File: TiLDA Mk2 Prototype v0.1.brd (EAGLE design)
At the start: 68 x 100 mm, 215 parts, among them IC1 ATSAM3X8EA-AU, IC2 MPU-6050, IC3 SRF-V1.2, IC4 LTC4160, IC5 S25FL216K0PMFI011, IC6 AT45DB161E-SSHFHA (NP), IC7 HMC5883LSMD (NP), IC8 MCP1825T-3302E/DC, J1 ZX62-AB-5PA(11), J2 FCI 62684-401100ALF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

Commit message: Prototype: Part Value updates Gerbers: update to latest PDF: update to latest
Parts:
- C1, C10: value 0805/2.2u/10V/Y5V -> 0805/2u2/10V/Y5V
- C11, C12, C14, C17, C18, C19, C20: value 0805/2.2u/16V/Y5V -> 0805/2u2/16V/Y5V
- C13, C15, C16, C22, C23: value 0805/2.2u/25V/Y5V -> 0805/2u2/25V/Y5V
- C28: value 0603/4u7/10V/Y5V -> 0603/4u7/6V3/Y5V
- C30, C35: value 0805/10u/6.3V/X5R -> 0805/10u/6V3/X5R
- C5: value 0402/2.2n/50V/X7R -> 0402/2n2/50V/X7R
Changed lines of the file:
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@@
 <text x="43.1" y="32.5" size="0.8128" layer="22" ratio="15" rot="MR90">IC7</text>
 <text x="14.1" y="38.8" size="0.8128" layer="22" ratio="15" rot="MR0">IC3</text>
-<text x="12.3" y="4.9" size="0.8128" layer="22" ratio="15" rot="MR90">IC4</text>
+<text x="13" y="5.4" size="0.8128" layer="22" ratio="15" rot="MR90">IC4</text>
 <text x="20.2" y="71.8" size="0.8128" layer="22" ratio="15" rot="MR90">IC5</text>
 <text x="20.2" y="78.4" size="0.8128" layer="22" ratio="15" rot="MR90">IC6</text>
@@
 <element name="J2" library="TiLDA Mk2 Parts" package="62684-401100" value="FCI 62684-401100ALF" x="42.3" y="7.9" rot="MR180"/>
 <element name="R3" library="TiLDA Mk2 Parts" package="R0402-ARDUINO-ROUND" value="0402/0R/5%/(NP)" x="34.1" y="14.2" rot="MR270"/>
-<element name="C10" library="TiLDA Mk2 Parts" package="C0805K" value="0805/2.2u/10V/Y5V" x="34.3" y="17" rot="MR90"/>
-<element name="C11" library="TiLDA Mk2 Parts" package="C0805K" value="0805/2.2u/16V/Y5V" x="36.3" y="15" rot="MR90"/>
-<element name="C12" library="TiLDA Mk2 Parts" package="C0805K" value="0805/2.2u/16V/Y5V" x="36.3" y="19" rot="MR90"/>
-<element name="C13" library="TiLDA Mk2 Parts" package="C0805K" value="0805/2.2u/25V/Y5V" x="36.3" y="22.9" rot="MR90"/>
-<element name="C14" library="TiLDA Mk2 Parts" package="C0805K" value="0805/2.2u/16V/Y5V" x="39.3" y="22.9" rot="MR270"/>
-<element name="C15" library="TiLDA Mk2 Parts" package="C0805K" value="0805/2.2u/25V/Y5V" x="40.3" y="15" rot="MR90"/>
-<element name="C16" library="TiLDA Mk2 Parts" package="C0805K" value="0805/2.2u/25V/Y5V" x="40.3" y="19" rot="MR270"/>
-<element name="C17" library="TiLDA Mk2 Parts" package="C0805K" value="0805/2.2u/16V/Y5V" x="41.3" y="22.9" rot="MR270"/>
-<element name="C18" library="TiLDA Mk2 Parts" package="C0805K" value="0805/2.2u/16V/Y5V" x="43.7" y="15" rot="MR270"/>
-<element name="C19" library="TiLDA Mk2 Parts" package="C0805K" value="0805/2.2u/16V/Y5V" x="43.7" y="18.9" rot="MR270"/>
-<element name="C20" library="TiLDA Mk2 Parts" package="C0805K" value="0805/2.2u/16V/Y5V" x="44.6" y="22" rot="MR0"/>
+<element name="C10" library="TiLDA Mk2 Parts" package="C0805K" value="0805/2u2/10V/Y5V" x="34.3" y="17" rot="MR90"/>
+<element name="C11" library="TiLDA Mk2 Parts" package="C0805K" value="0805/2u2/16V/Y5V" x="36.3" y="15" rot="MR90"/>
+<element name="C12" library="TiLDA Mk2 Parts" package="C0805K" value="0805/2u2/16V/Y5V" x="36.3" y="19" rot="MR90"/>
+<element name="C13" library="TiLDA Mk2 Parts" package="C0805K" value="0805/2u2/25V/Y5V" x="36.3" y="22.9" rot="MR90"/>
+<element name="C14" library="TiLDA Mk2 Parts" package="C0805K" value="0805/2u2/16V/Y5V" x="39.3" y="22.9" rot="MR270"/>
+<element name="C15" library="TiLDA Mk2 Parts" package="C0805K" value="0805/2u2/25V/Y5V" x="40.3" y="15" rot="MR90"/>
+<element name="C16" library="TiLDA Mk2 Parts" package="C0805K" value="0805/2u2/25V/Y5V" x="40.3" y="19" rot="MR270"/>
+<element name="C17" library="TiLDA Mk2 Parts" package="C0805K" value="0805/2u2/16V/Y5V" x="41.3" y="22.9" rot="MR270"/>
+<element name="C18" library="TiLDA Mk2 Parts" package="C0805K" value="0805/2u2/16V/Y5V" x="43.7" y="15" rot="MR270"/>
+<element name="C19" library="TiLDA Mk2 Parts" package="C0805K" value="0805/2u2/16V/Y5V" x="43.7" y="18.9" rot="MR270"/>
+<element name="C20" library="TiLDA Mk2 Parts" package="C0805K" value="0805/2u2/16V/Y5V" x="44.6" y="22" rot="MR0"/>
 <element name="R9" library="TiLDA Mk2 Parts" package="R0402-ARDUINO-ROUND" value="0402/2K/5%" x="46.9" y="12.9" rot="MR270"/>
 <element name="C21" library="TiLDA Mk2 Parts" package="C0603-ROUND" value="0603/1u/10V/X5R" x="47.5" y="16.6" rot="MR90"/>
-<element name="C22" library="TiLDA Mk2 Parts" package="C0805K" value="0805/2.2u/25V/Y5V" x="50.6" y="15.8" rot="MR90"/>
-<element name="C23" library="TiLDA Mk2 Parts" package="C0805K" value="0805/2.2u/25V/Y5V" x="52.55" y="15.8" rot="MR90"/>
+<element name="C22" library="TiLDA Mk2 Parts" package="C0805K" value="0805/2u2/25V/Y5V" x="50.6" y="15.8" rot="MR90"/>
+<element name="C23" library="TiLDA Mk2 Parts" package="C0805K" value="0805/2u2/25V/Y5V" x="52.55" y="15.8" rot="MR90"/>
 <element name="C24" library="TiLDA Mk2 Parts" package="C0603-ROUND" value="0603/1u/10V/X5R" x="54.4" y="12.75" rot="MR180"/>
 <element name="C25" library="TiLDA Mk2 Parts" package="C0603-ROUND" value="0603/1u/10V/X5R" x="56.85" y="12.7" rot="MR90"/>
@@
 <element name="JP6" library="TiLDA Mk2 Parts" package="1X06" value="FTDI" x="65.8" y="77.7" rot="MR270"/>
 <element name="SG1" library="TiLDA Mk2 Parts" package="BUZZER-PKLCS1212E" value="PKLCS1212E4001-R1" x="48" y="91.3" rot="MR180"/>
-<element name="C1" library="TiLDA Mk2 Parts" package="C0805K" value="0805/2.2u/10V/Y5V" x="48.5" y="20.3" rot="MR0"/>
+<element name="C1" library="TiLDA Mk2 Parts" package="C0805K" value="0805/2u2/10V/Y5V" x="48.5" y="20.3" rot="MR0"/>
 <element name="R13" library="TiLDA Mk2 Parts" package="R0402-ARDUINO-ROUND" value="0402/0R/5%" x="49.05" y="21.8" rot="MR180"/>
 <element name="R2" library="TiLDA Mk2 Parts" package="R0402-ARDUINO-ROUND" value="0402/33K/5%/(NP)" x="47.2" y="21.8" rot="MR180"/>
@@
 </element>
 <element name="C4" library="TiLDA Mk2 Parts" package="C0402-ARDUINO-ROUND" value="0402/100n/10V/X5R" x="30.5" y="32.7" rot="MR90"/>
-<element name="C5" library="TiLDA Mk2 Parts" package="C0402-ARDUINO-ROUND" value="0402/2.2n/50V/X7R" x="32.8" y="37.35" rot="MR0"/>
+<element name="C5" library="TiLDA Mk2 Parts" package="C0402-ARDUINO-ROUND" value="0402/2n2/50V/X7R" x="32.8" y="37.35" rot="MR0"/>
 <element name="C6" library="TiLDA Mk2 Parts" package="C0402-ARDUINO-ROUND" value="0402/100n/10V/X5R" x="33.2" y="30" rot="MR0"/>
 <element name="Q1" library="TiLDA Mk2 Parts" package="SOT23-R" value="DMG2301U" x="45.2" y="24.9" rot="MR90"/>
@@
 <element name="L1" library="TiLDA Mk2 Parts" package="LPS4018" value="LPS4018-332MLB" x="21.3" y="7.75" rot="MR270"/>
 <element name="Q12" library="TiLDA Mk2 Parts" package="SOT23-R" value="SI2333DS-T1-E3" x="21.2" y="12" rot="MR270"/>
-<element name="C35" library="TiLDA Mk2 Parts" package="C0805RND" value="0805/10u/6.3V/X5R" x="18.6" y="13.1" rot="MR270"/>
+<element name="C35" library="TiLDA Mk2 Parts" package="C0805RND" value="0805/10u/6V3/X5R" x="18.6" y="13.1" rot="MR270"/>
 <element name="C36" library="TiLDA Mk2 Parts" package="C0805RND" value="0805/22u/25V/X5R" x="25.9" y="9.85" rot="MR0"/>
 <element name="R27" library="TiLDA Mk2 Parts" package="R0402-ARDUINO-ROUND" value="0402/100K/1%" x="15.45" y="4.6" rot="MR180"/>
@@
 <element name="IC7" library="TiLDA Mk2 Parts" package="16LPCC" value="HMC5883LSMD (NP)" x="39.7" y="33.5" rot="MR90"/>
 <element name="C27" library="TiLDA Mk2 Parts" package="C0402-ARDUINO-ROUND" value="0402/100n/10V/X5R" x="39.5" y="29.65" rot="MR180"/>
-<element name="C28" library="TiLDA Mk2 Parts" package="C0603-ROUND" value="0603/4u7/10V/Y5V" x="40.45" y="36.85" rot="MR0"/>
+<element name="C28" library="TiLDA Mk2 Parts" package="C0603-ROUND" value="0603/4u7/6V3/Y5V" x="40.45" y="36.85" rot="MR0"/>
 <element name="C31" library="TiLDA Mk2 Parts" package="C0402-ARDUINO-ROUND" value="0402/0u22/10V/X5R" x="38.2" y="37" rot="MR270"/>
 <element name="JP7" library="TiLDA Mk2 Parts" package="2X8" value="ETH" x="24.88" y="76.677" rot="MR90"/>
@@
 <element name="R32" library="TiLDA Mk2 Parts" package="R0402-ARDUINO-ROUND" value="0402/0R/5%" x="63.2" y="71.48" rot="MR0"/>
 <element name="SJ6" library="TiLDA Mk2 Parts" package="SJ_2S-NO" value="RESET BUTTON" x="40.6" y="84.1" rot="MR0"/>
-<element name="C30" library="TiLDA Mk2 Parts" package="C0805RND" value="0805/10u/6.3V/X5R" x="30.2" y="15.6" rot="MR90"/>
+<element name="C30" library="TiLDA Mk2 Parts" package="C0805RND" value="0805/10u/6V3/X5R" x="30.2" y="15.6" rot="MR90"/>
 <element name="R26" library="TiLDA Mk2 Parts" package="R0402-ARDUINO-ROUND" value="0402/10K/5%" x="27.65" y="11.55" rot="MR180"/>
 <element name="IC6" library="TiLDA Mk2 Parts" package="SO08-EIAJ" value="AT45DB161E-SSHFHA (NP)" x="16.4" y="78.9" rot="MR180"/>

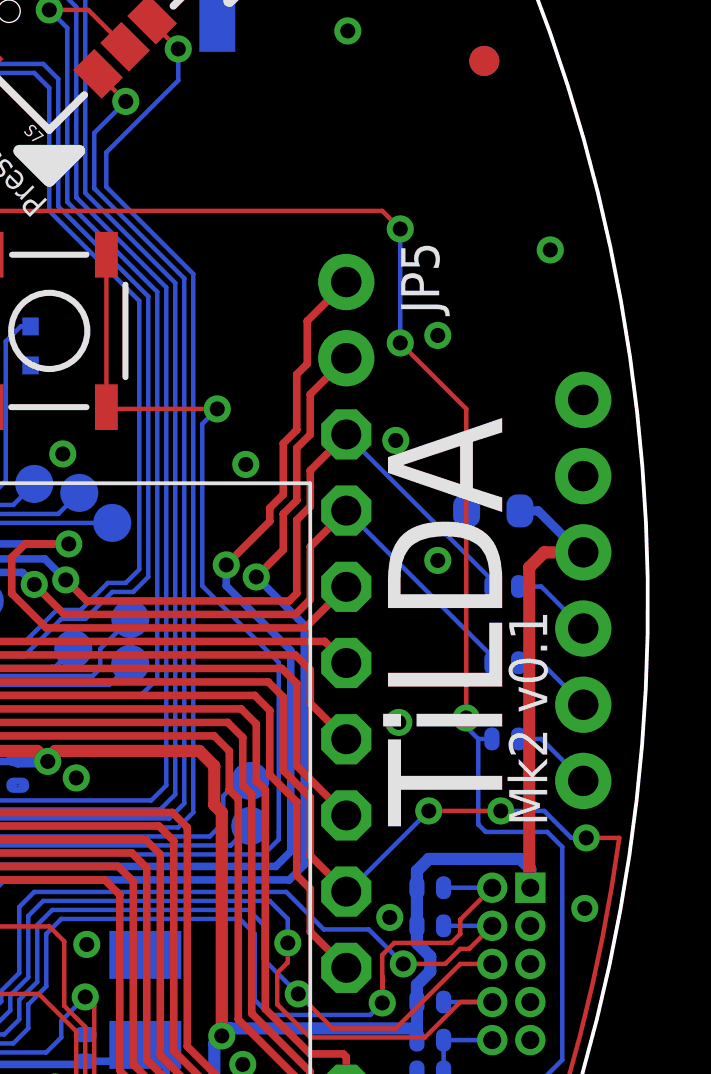
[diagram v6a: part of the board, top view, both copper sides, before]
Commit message: Prototype: FTDI Power Jumper
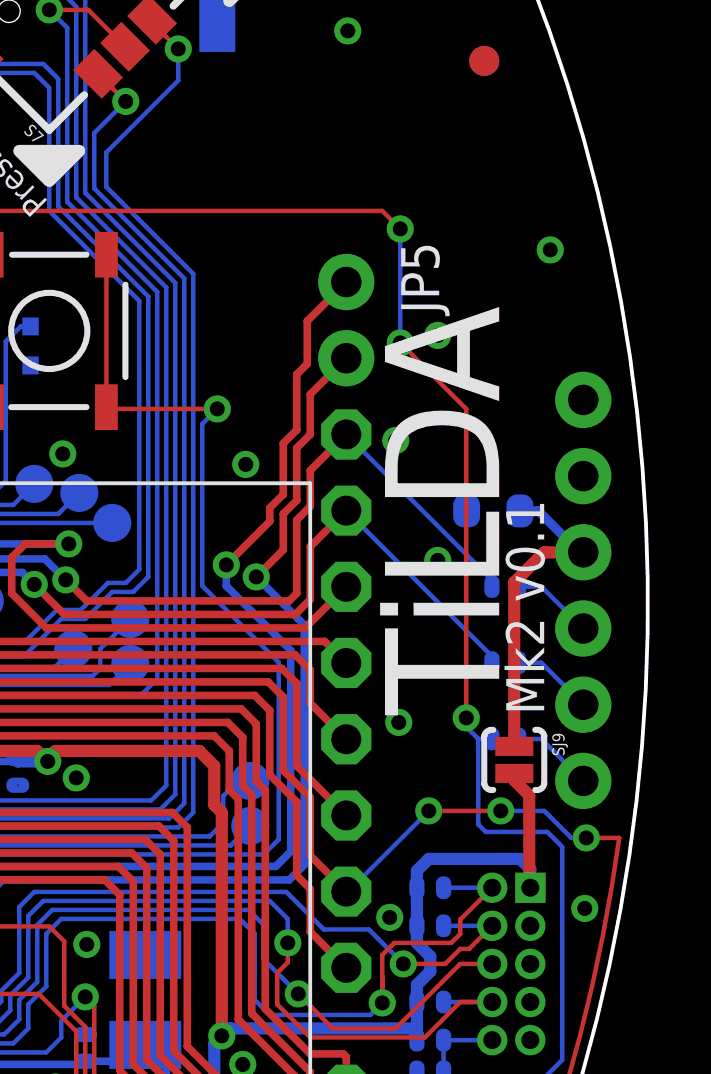
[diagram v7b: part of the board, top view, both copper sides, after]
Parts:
- added SJ9: FTDI Power, TiLDA Mk2 Parts:SJ_2S-NO
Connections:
- new net FTDI_PWR: C38.2, JP6.3, SJ9.1
- net 3V3: now also SJ9.2; no longer C38.2, JP6.3
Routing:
- net 3V3: track 459.5 -> 448.1 mm
- net FTDI_PWR: track 0.00 -> 10.9 mm
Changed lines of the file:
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@@
 <text x="23.75" y="43.1" size="0.6096" layer="22" ratio="15" rot="MR90">Ext | 3V3</text>
 <text x="20.45" y="44.2" size="0.6096" layer="22" ratio="15" rot="MR90">ARef</text>
-<text x="64.6" y="63.5" size="1.27" layer="21" ratio="15" rot="R90">Mk2 v0.1</text>
-<text x="63.1" y="63.5" size="3.81" layer="21" ratio="20" rot="R90">TiLDA</text>
+<text x="64.5" y="67.2" size="1.27" layer="21" ratio="15" rot="R90">Mk2 v0.1</text>
+<text x="63" y="67.2" size="3.81" layer="21" ratio="20" rot="R90">TiLDA</text>
 <text x="62.9" y="6.5" size="0.8128" layer="21" ratio="15" rot="R90">IR_TX</text>
 <text x="23.6" y="0.8" size="0.8128" layer="21" ratio="15" rot="R90">IR_RX</text>
@@
 <element name="C37" library="TiLDA Mk2 Parts" package="C0805RND" value="0805/22u/25V/X5R" x="57.1" y="3.6" rot="MR270"/>
 <element name="C38" library="TiLDA Mk2 Parts" package="C0603-ROUND" value="0603/1u/10V/X5R" x="62.8" y="74" rot="MR180"/>
+<element name="SJ9" library="TiLDA Mk2 Parts" package="SJ_2S-NO" value="FTDI Power" x="63.5" y="65.7" rot="R270"/>
 </elements>
 <signals>
@@
 <contactref element="Q8" pad="2"/>
 <contactref element="JP1" pad="2"/>
-<contactref element="JP6" pad="3"/>
 <contactref element="JP2" pad="1"/>
 <contactref element="J5" pad="P4"/>
@@
 <wire x1="14.8055" y1="38.5" x2="14.8" y2="38.5" width="0.4064" layer="16"/>
 <via x="47.95" y="65.65" extent="1-16" drill="0.5"/>
-<wire x1="65.8" y1="72.62" x2="64.5" y2="72.62" width="0.4064" layer="1"/>
-<wire x1="64.5" y1="72.62" x2="64" y2="72.12" width="0.4064" layer="1"/>
-<wire x1="64" y1="72.12" x2="64" y2="61.45" width="0.4064" layer="1"/>
+<wire x1="64" y1="64.52" x2="64" y2="61.45" width="0.4064" layer="1"/>
 <wire x1="64.035" y1="61.44" x2="64.01" y2="61.44" width="0.4064" layer="1"/>
 <wire x1="64.01" y1="61.44" x2="64" y2="61.45" width="0.4064" layer="1"/>
@@
 <contactref element="C37" pad="1"/>
 <wire x1="57.1" y1="4.577" x2="57.1" y2="5" width="0.3084" layer="16"/>
-<contactref element="C38" pad="2"/>
-<wire x1="63.689" y1="74" x2="64.3" y2="74" width="0.3084" layer="16"/>
-<wire x1="64.3" y1="74" x2="65.68" y2="72.62" width="0.3084" layer="16"/>
-<wire x1="65.68" y1="72.62" x2="65.8" y2="72.62" width="0.3084" layer="16"/>
 <wire x1="30.2" y1="14.623" x2="30.7" y2="14.623" width="0.4064" layer="16"/>
 <wire x1="30.7" y1="14.623" x2="30.7" y2="14.6" width="0.4064" layer="16"/>
 <wire x1="30.2" y1="14.623" x2="29.881" y2="14.623" width="0.4064" layer="16"/>
 <wire x1="29.881" y1="14.623" x2="29.881" y2="14.63" width="0.4064" layer="16"/>
+<contactref element="SJ9" pad="2"/>
+<wire x1="63.5" y1="65.25" x2="63.5" y2="65.02" width="0.4064" layer="1"/>
+<wire x1="63.5" y1="65.02" x2="64" y2="64.52" width="0.4064" layer="1"/>
 </signal>
 <signal name="GND">
@@
 <signal name="F1">
 </signal>
+<signal name="FTDI_PWR">
+<contactref element="JP6" pad="3"/>
+<contactref element="C38" pad="2"/>
+<contactref element="SJ9" pad="1"/>
+<wire x1="65.8" y1="72.62" x2="64.5" y2="72.62" width="0.4064" layer="1"/>
+<wire x1="63.689" y1="74" x2="64.3" y2="74" width="0.3084" layer="16"/>
+<wire x1="64.3" y1="74" x2="65.68" y2="72.62" width="0.3084" layer="16"/>
+<wire x1="65.68" y1="72.62" x2="65.8" y2="72.62" width="0.3084" layer="16"/>
+<wire x1="64.5" y1="72.62" x2="63.5" y2="71.62" width="0.4064" layer="1"/>
+<wire x1="63.5" y1="71.62" x2="63.5" y2="66.15" width="0.4064" layer="1"/>
+</signal>
 </signals>
